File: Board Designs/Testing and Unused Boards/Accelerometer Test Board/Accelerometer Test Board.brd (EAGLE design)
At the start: 30.1 x 27 mm, 6 parts

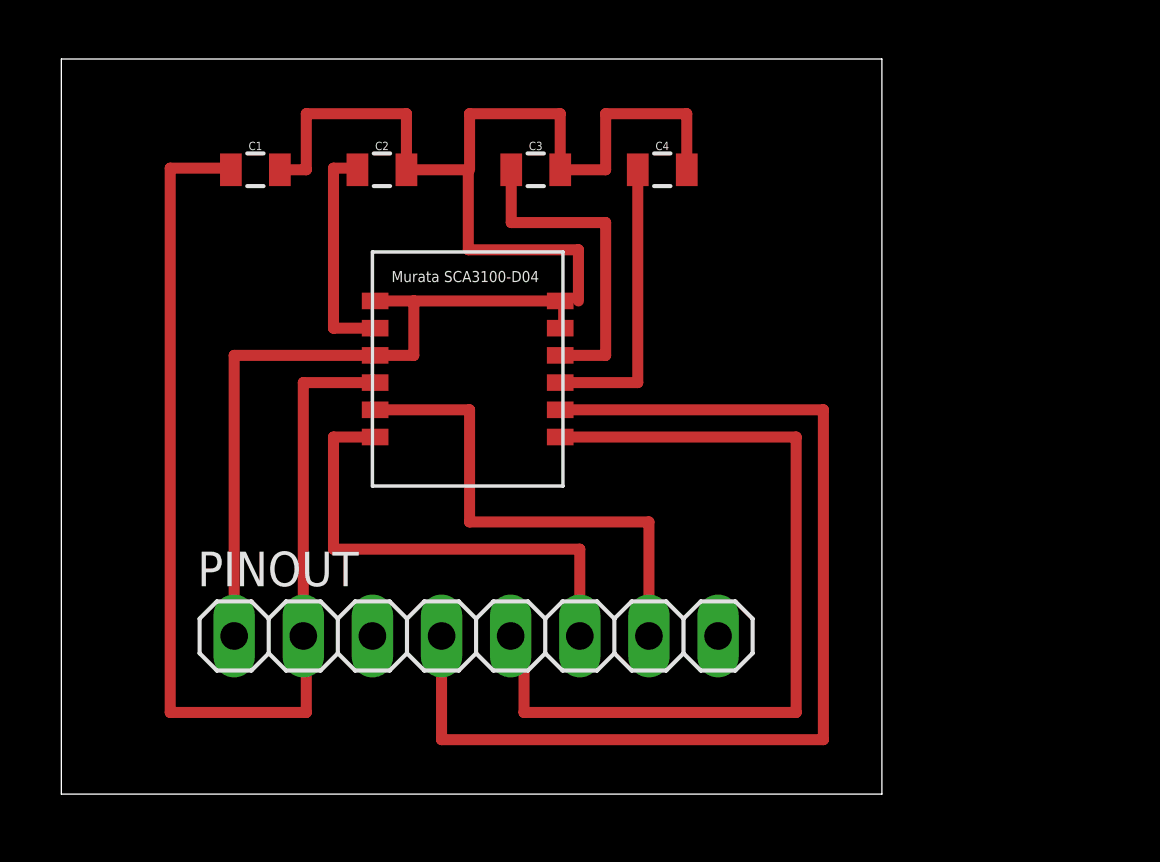
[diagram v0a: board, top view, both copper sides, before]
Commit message: Updated Accelerometer Board
Connected VDIO to VDD
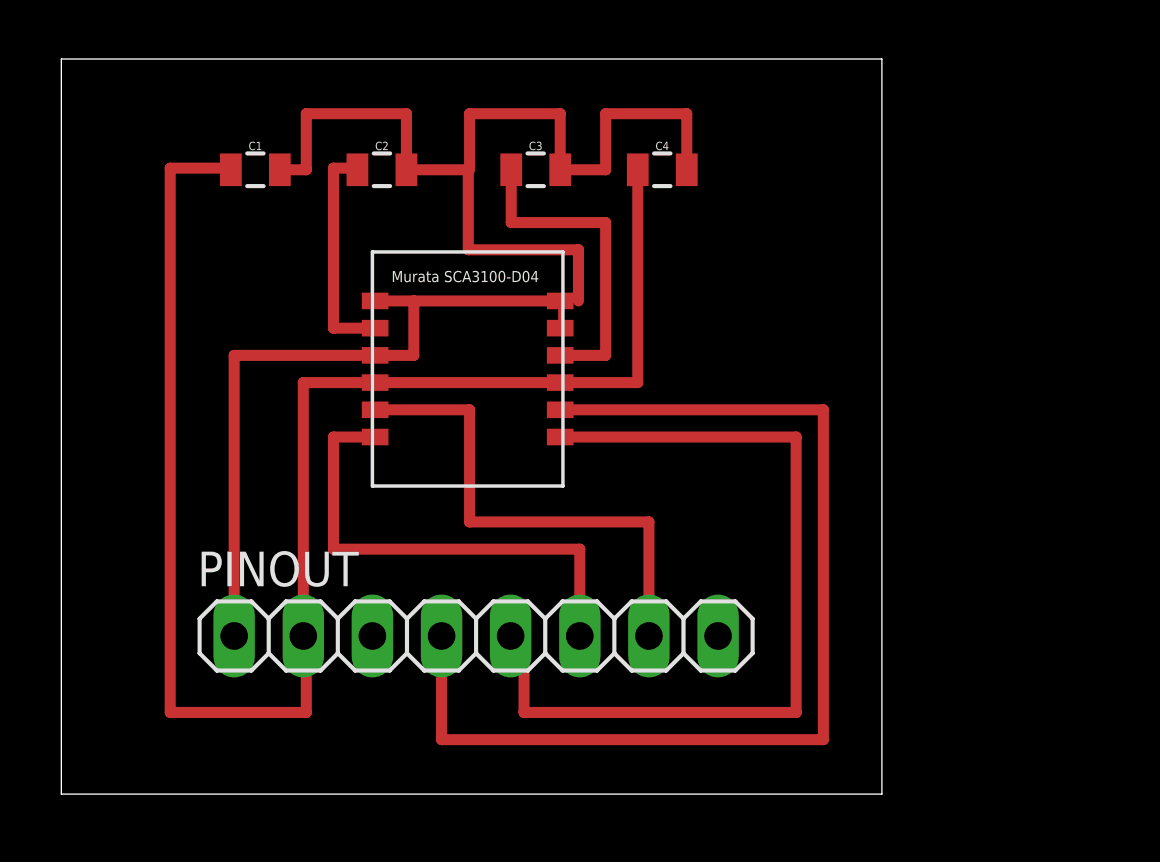
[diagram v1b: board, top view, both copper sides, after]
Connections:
- removed net N$4: C4.1, U$1.DVIO
- net VDD: now also C4.1, U$1.DVIO
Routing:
- net VDD: track 42.2 -> 59.7 mm
- net N$4: track 10.8 -> 0.00 mm
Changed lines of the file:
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@@
 <wire x1="16.53" y1="21" x2="16.53" y2="22.94" width="0.4064" layer="1"/>
-</signal>
-<signal name="N$4">
-<contactref element="U$1" pad="DVIO"/>
-<contactref element="C4" pad="1"/>
-<wire x1="18.33" y1="15" x2="18.33" y2="15.12" width="0.1524" layer="1"/>
-<wire x1="18.33" y1="15.12" x2="21.18" y2="15.12" width="0.4064" layer="1"/>
-<wire x1="21.18" y1="15.12" x2="21.18" y2="22.94" width="0.4064" layer="1"/>
 </signal>
 <signal name="N$5">
@@
 <contactref element="C1" pad="1"/>
 <contactref element="U$1" pad="VDD"/>
-<wire x1="11.53" y1="15.12" x2="8.89" y2="15.12" width="0.4064" layer="1"/>
+<wire x1="8.89" y1="15.12" x2="11.53" y2="15.12" width="0.4064" layer="1"/>
 <wire x1="8.89" y1="15.12" x2="8.89" y2="5.81" width="0.4064" layer="1"/>
 <wire x1="8.89" y1="5.81" x2="9" y2="5.81" width="0.1524" layer="1"/>
@@
 <wire x1="4" y1="23" x2="6.23" y2="23" width="0.4064" layer="1"/>
 <wire x1="6.23" y1="23" x2="6.23" y2="22.94" width="0.1524" layer="1"/>
+<contactref element="U$1" pad="DVIO"/>
+<contactref element="C4" pad="1"/>
+<wire x1="18.33" y1="15.12" x2="18.33" y2="15" width="0.1524" layer="1"/>
+<wire x1="18.33" y1="15.12" x2="21.18" y2="15.12" width="0.4064" layer="1"/>
+<wire x1="21.18" y1="15.12" x2="21.18" y2="22.94" width="0.4064" layer="1"/>
+<wire x1="11.53" y1="15.12" x2="18.33" y2="15.12" width="0.4064" layer="1"/>
 </signal>
 </signals>

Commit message: Reconfigured board based on new datasheet
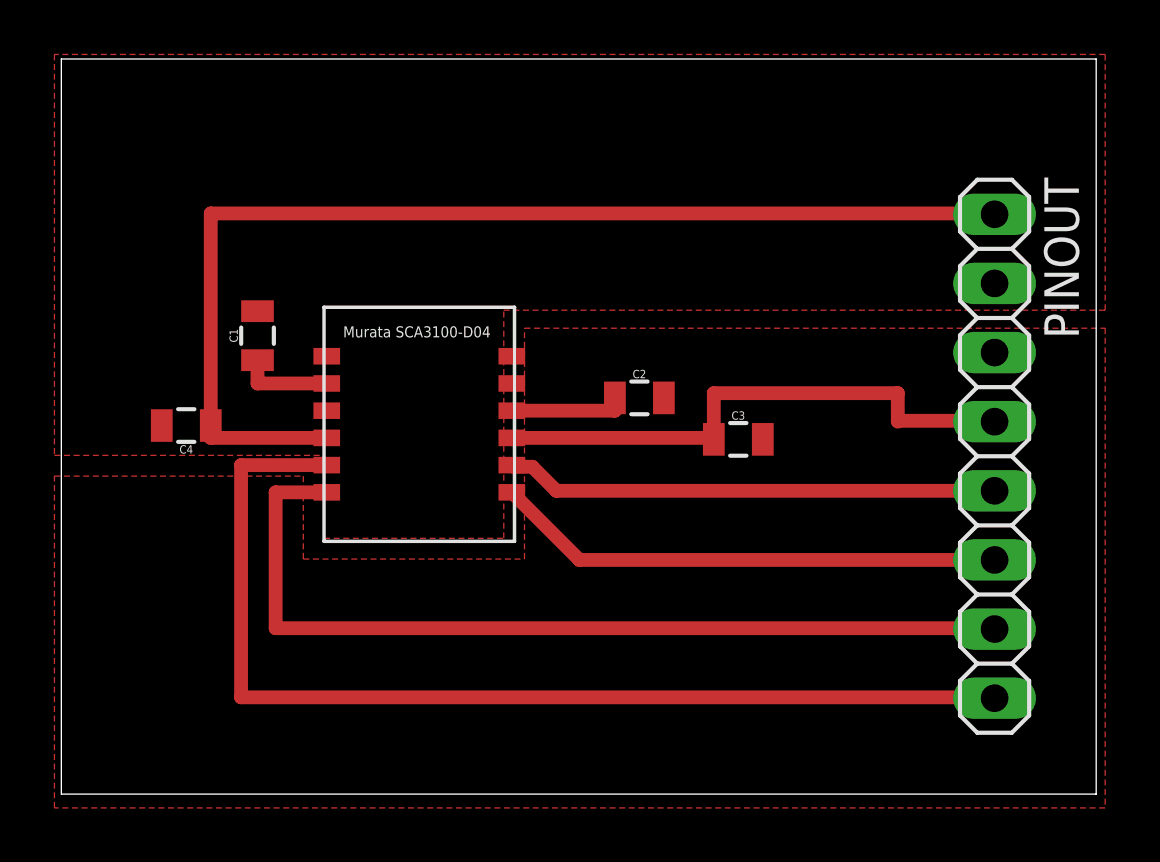
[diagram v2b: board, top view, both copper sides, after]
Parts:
- moved PINOUT 20.2 mm to (34.3, 12.4), turned to 270 degrees
- moved C4 19.9 mm to (4.59, 13.5), turned to 180 degrees
- moved C2 12.6 mm to (21.2, 14.6)
- moved C3 12.4 mm to (24.9, 13.0)
- moved C1 6.10 mm to (7.21, 16.8), turned to 90 degrees
- moved U$1 2.70 mm to (9.65, 17.9)
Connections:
- removed net N$5: PINOUT.5, U$1.MOSI
- removed net N$6: PINOUT.4, U$1.SCK
- removed net N$7: PINOUT.7, U$1.CSB
- removed net N$8: PINOUT.6, U$1.MISO
- new net AGND: C1.2, C4.2, PINOUT.2, U$1.AVSS, U$1.EMC_GND, U$1.RESERVED
- new net CSB: PINOUT.8, U$1.CSB
- new net DVIO: C3.1, PINOUT.4, U$1.DVIO
- new net MISO: PINOUT.7, U$1.MISO
- new net MOSI: PINOUT.6, U$1.MOSI
- new net SCK: PINOUT.5, U$1.SCK
- net GND: now also PINOUT.3; no longer C1.2, C4.2, PINOUT.1, U$1.AVSS, U$1.EMC_GND, U$1.RESERVED
- net N$1: now also C1.1; no longer C2.1
- net N$3: now also C2.1; no longer C3.1
- net VDD: now also PINOUT.1; no longer C1.1, PINOUT.2, U$1.DVIO
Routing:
- net GND: track 63.6 -> 0.00 mm
- net N$6: track 39.6 -> 0.00 mm
- net CSB: track 0.00 -> 39.4 mm
- net MISO: track 0.00 -> 33.3 mm
- net N$5: track 32.1 -> 0.00 mm
- net DVIO: track 0.00 -> 20.6 mm
- net MOSI: track 0.00 -> 18.8 mm
- net VDD: track 59.7 -> 41.3 mm
- net N$7: track 18.4 -> 0.00 mm
- net SCK: track 0.00 -> 18.1 mm
- net N$8: track 17.9 -> 0.00 mm
- net N$3: track 12.1 -> 4.26 mm
- net N$1: track 8.35 -> 3.40 mm
- added copper zone on layer 1, net AGND
- added copper zone on layer 1, net GND
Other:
- board size 30.1 x 27 mm -> 38 x 27 mm
